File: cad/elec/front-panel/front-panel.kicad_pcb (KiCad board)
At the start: 2 copper layers, 182 x 20 mm, 22 parts, among them P1 CONN_01X10, U1 FSM2JAH, U2 FSM2JAH, U3 FSM2JAH

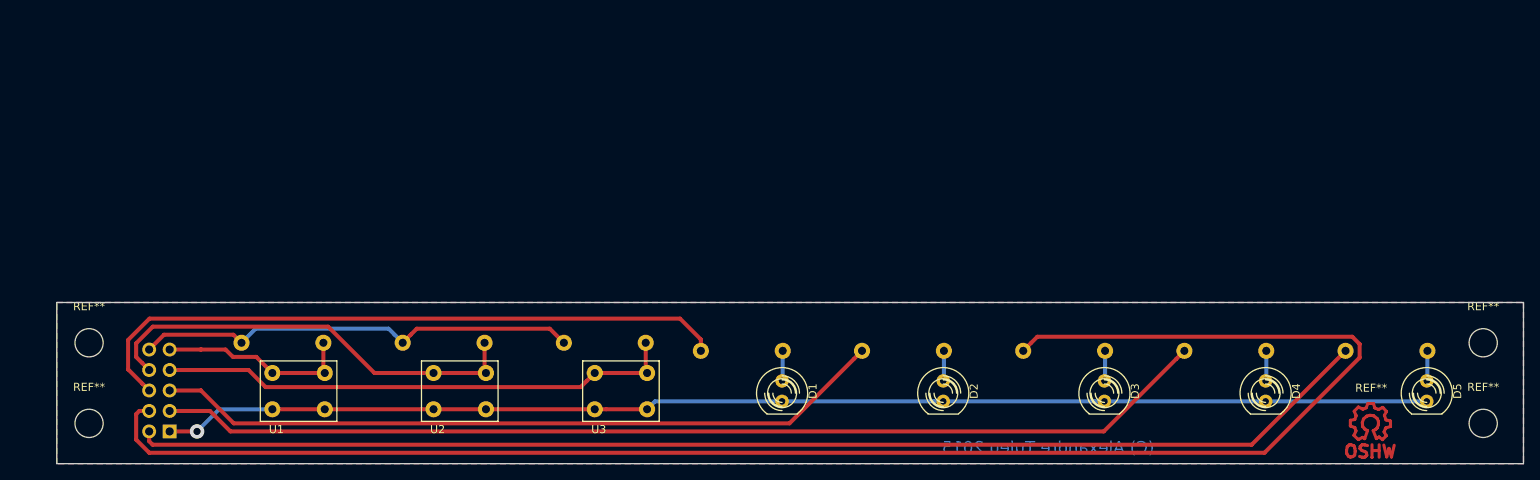
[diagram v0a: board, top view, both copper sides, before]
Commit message: Makes the board ready for manual engraving
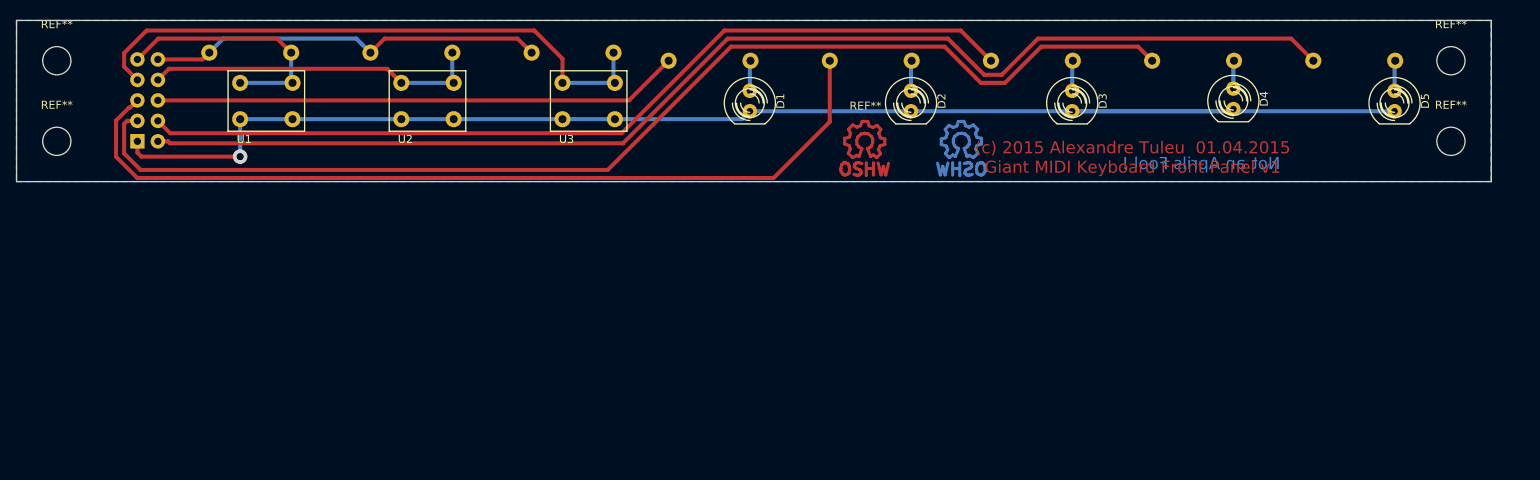
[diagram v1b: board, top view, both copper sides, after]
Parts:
- removed the REF** at (213.0, 95.0)
- added REF**: Symbol_OSHW-Logo_CopperTop, Symbols:Symbol_OSHW-Logo_CopperTop, F.Cu at (150.2, 60.0)
- added REF**: Symbol_OSHW-Logo_CopperTop, Symbols:Symbol_OSHW-Logo_CopperTop, B.Cu at (162.2, 60.0)
- D1, D2, D3, D4, D5: footprint LEDs:LED-5MM -> Giant Midi Keyboard:LED-5MM
- P1: footprint Socket_Strips:Socket_Strip_Straight_2x05 -> Giant Midi Keyboard:Header_2x5
- moved P1 41.2 mm to (61.3, 54.9), turned to 180 degrees
- moved D4 36.5 mm to (196.0, 54.7)
- moved D1 36.2 mm to (136.0, 55.0)
- moved D2 36.2 mm to (156.0, 55.0)
- moved D3 36.2 mm to (176.0, 55.0)
- moved D5 36.2 mm to (216.0, 55.0)
- moved R1 36.2 mm to (114.0, 49.0)
- moved R2 36.2 mm to (94.0, 49.0)
- moved R3 36.2 mm to (131.0, 50.0)
- moved R4 36.2 mm to (151.0, 50.0)
- moved R5 36.2 mm to (171.0, 50.0)
- moved R6 36.2 mm to (191.0, 50.0)
- moved R7 36.2 mm to (211.0, 50.0)
- moved R8 36.2 mm to (74.0, 49.0)
- moved U1 36.2 mm to (76.0, 55.0)
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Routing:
- net Net-(P1-Pad4): track 206.9 -> 110.9 mm
- net GND: track 157.5 -> 182.7 mm
- net Net-(P1-Pad5): track 91.4 -> 108.3 mm
- net Net-(P1-Pad6): track 82.0 -> 65.4 mm
- net Net-(P1-Pad3): track 131.1 -> 144.7 mm
- net Net-(P1-Pad8): track 54.4 -> 41.8 mm
- net Net-(P1-Pad7): track 64.7 -> 74.3 mm
- net Net-(P1-Pad9): track 24.3 -> 31.2 mm
- net +5V: track 55.5 -> 49.6 mm
- net Net-(P1-Pad2): track 154.7 -> 153.7 mm
- removed copper zone on F.Cu, net GND
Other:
- board size 182 x 20 mm -> 183 x 20 mm
- board text added: "(c) 2015 Alexandre Tuleu 01.04.2015 Giant MIDI Keyboard Front Panel v1"
- board text added: "Not an Aprils Fool !"
- board text removed: "(C) Alexandre Tuleu 2015"
